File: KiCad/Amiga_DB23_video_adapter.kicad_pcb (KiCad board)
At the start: 4 copper layers, 34.6 x 25 mm, 32 parts, among them J1 DB23_Female, J2 Conn_01x06, J3 Conn_01x06, J4 Conn_01x02, J5 Conn_01x02, J6 Conn_01x02, SW1 SW_SPDT, U1 74HCT2G17, U2 74HCT2G14, U3 THS7374IPWR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

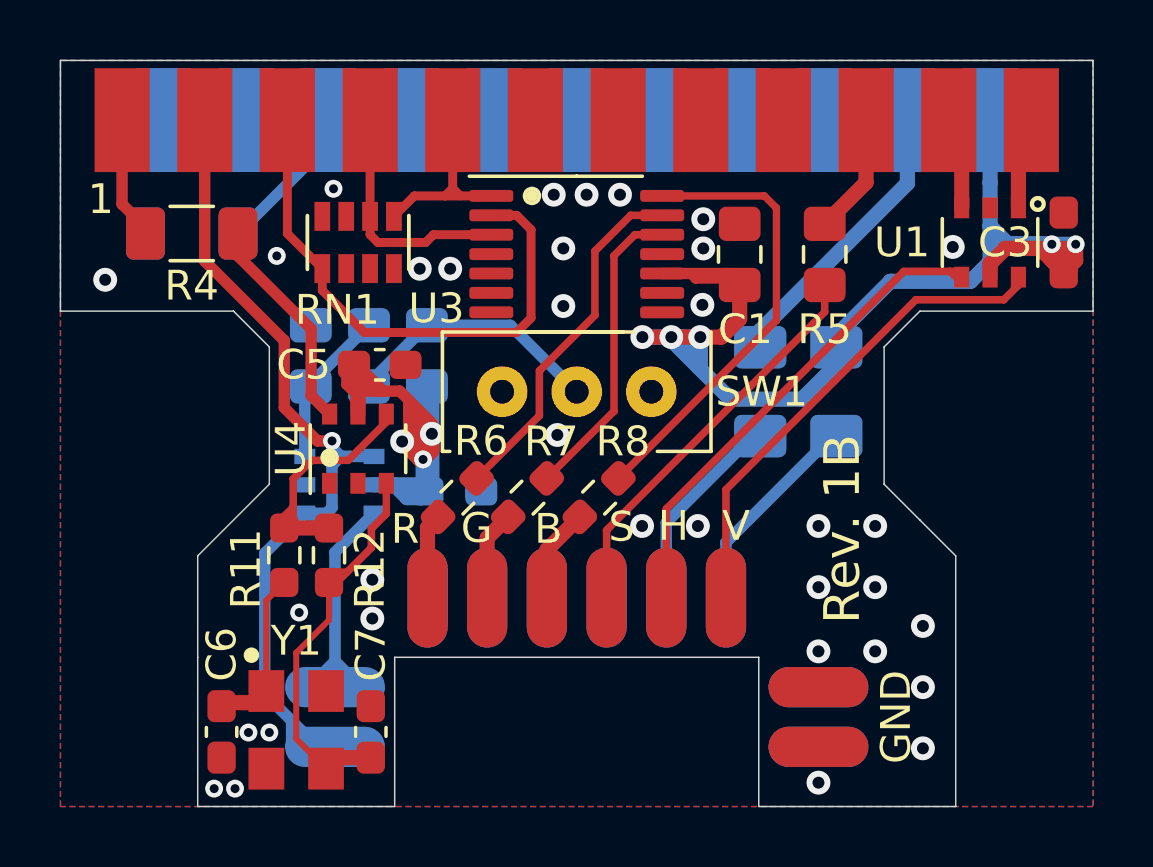
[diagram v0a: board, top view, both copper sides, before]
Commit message: Small fix of physical size to better fit the plastic DB23 shell, bump to Rev 1C
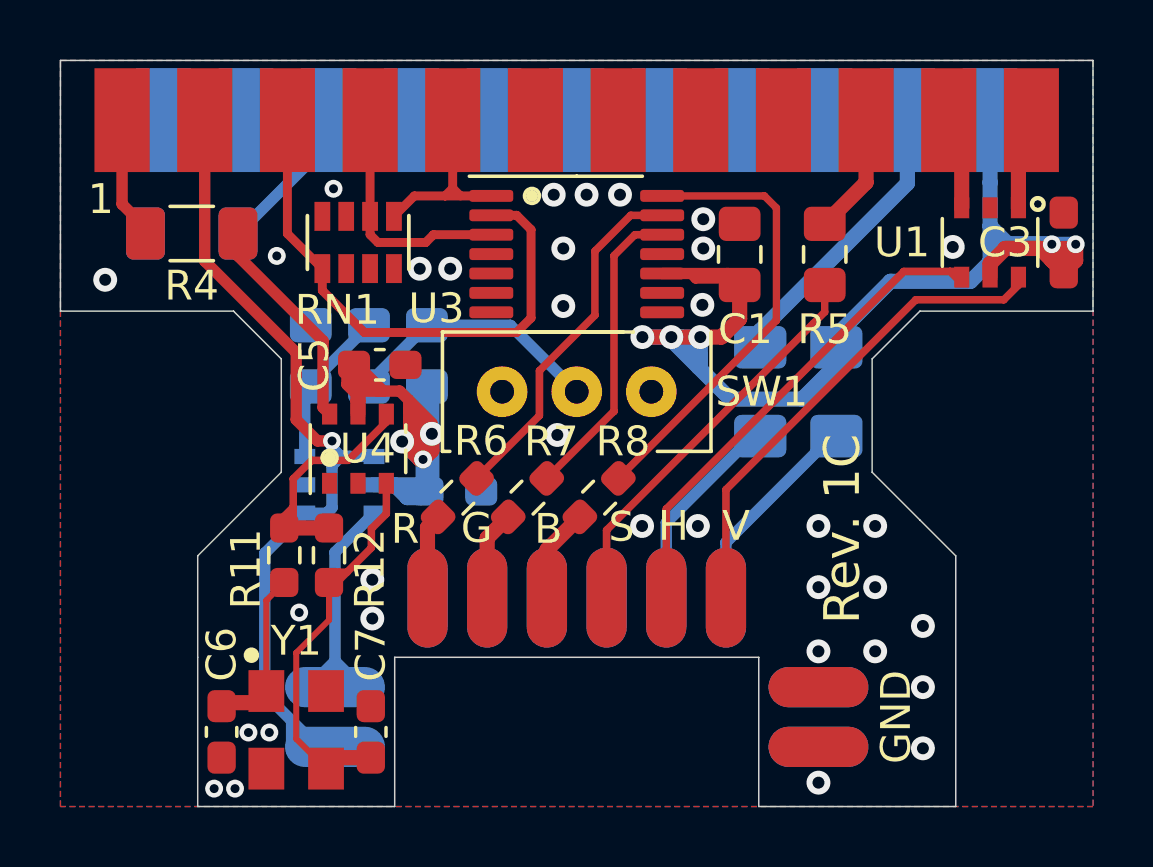
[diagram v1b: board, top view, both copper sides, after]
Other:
- outline, holes or cut-outs redrawn
- board text added: "Rev. 1C"
- board text removed: "Rev. 1B"
